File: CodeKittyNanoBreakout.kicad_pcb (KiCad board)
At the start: 2 copper layers, 17.8 x 43.2 mm, 14 parts, among them P1 CONN_01X02, P2 CONN_01X02, P3 CONN_01X03, P4 CONN_01X03, P5 CONN_01X02, SW1 SW_PUSH_SMALL_H, SW2 Switch_SPDT_x2, U1 ArduinoNano

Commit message: ...
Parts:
- added D2: D, Diodes_SMD:D_SOD-323_HandSoldering, F.Cu at (201.4, 113.5)
- added Q1: MMBT3904, TO_SOT_Packages_SMD:SOT-23, F.Cu at (210.3, 113.3)
- added R4: 1K, Resistors_SMD:R_0603_HandSoldering, F.Cu at (207.0, 113.4)
- P5: value CONN_01X02 -> CONN_01X03; footprint Pin_Headers:Pin_Header_Straight_1x02_Pitch2.54mm -> Pin_Headers:Pin_Header_Straight_1x03_Pitch2.54mm
- R1: footprint Resistors_SMD:R_0805_HandSoldering -> Resistors_SMD:R_0603_HandSoldering
- R2: footprint Resistors_SMD:R_0805_HandSoldering -> Resistors_SMD:R_0603_HandSoldering; moved to F.Cu
- SP1: value SPEAKER -> PIEZO
- moved F1 20.8 mm to (206.0, 113.9), turned to 180 degrees
- moved P5 10.5 mm to (208.9, 98.0), turned to 90 degrees
- moved G*** 9.25 mm to (205.2, 120.4)
- moved SP1 6.56 mm to (205.8, 120.9)
- moved P4 5.13 mm to (208.9, 100.6), turned to 90 degrees
- moved P3 4.13 mm to (208.9, 103.1), turned to 90 degrees
- moved P2 3.50 mm to (208.9, 95.5), turned to 90 degrees
- moved R1 1.67 mm to (210.2, 85.9), turned to 180 degrees
- moved P1 1.66 mm to (208.9, 93.0), turned to 90 degrees
- moved R2 0.92 mm to (210.2, 87.9), turned to 0 degrees
- moved U1 0.06 mm to (205.7, 104.1)
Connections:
- P5 pad 2: BUZZ -> 5V
- SP1 pad 1: BUZZ -> VCC
- SP1 pad 2: GND -> Net-(D2-Pad2)
- U1 pad 20: Net-(U1-Pad20) -> SENS
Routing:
- net Net-(F1-Pad1): track 7.31 -> 31.6 mm, vias 0 -> 4
- net Net-(D2-Pad2): track 0.00 -> 19.7 mm, vias 0 -> 1
- net GND: track 22.0 -> 7.86 mm
- net VCC: track 32.1 -> 20.9 mm
- net BUZZ: track 32.1 -> 21.1 mm, vias 1 -> 3
- net SENS: track 0.00 -> 10.4 mm, vias 0 -> 2
- net Net-(Q1-Pad1): track 0.00 -> 3.54 mm
- net RSERVO: track 15.2 -> 11.9 mm, vias 0 -> 1
- net RST: track 44.5 -> 41.7 mm, vias 2 -> 0
- net Net-(D1-Pad1): track 4.19 -> 2.31 mm
- net Net-(P1-Pad2): track 8.56 -> 6.84 mm, vias 1 -> 0
- net LSERVO: track 10.4 -> 11.7 mm, vias 0 -> 1
- net TAIL: track 3.95 -> 2.65 mm
- net 5V: track 36.8 -> 37.2 mm, vias 1 -> 2
- net Net-(P2-Pad2): track 8.66 -> 8.76 mm, vias 2 -> 0
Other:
- board text added: "CodeKitty v1.0 DM120317"
- board text removed: "-"
- board text removed: "1"
- board text removed: "BATT"
- board text removed: "CodeKitty DM100917"
- board text removed: "LEFT"
- board text removed: "RIGHT"
- board text removed: "SPKR"
- board text removed: "TAIL"

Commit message: changed DM to CK
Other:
- board text added: "CodeKitty v1.01 CK020318"
- board text removed: "CodeKitty v1.0 DM120317"
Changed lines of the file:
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@@
 (kicad_pcb (version 4) (host pcbnew 4.0.4-stable)
   (general
-    (links 32)
-    (no_connects 1)
-    (area 196.774999 82.474999 214.705001 125.805001)
+    (links 31)
+    (no_connects 0)
+    (area 194.564 75.9726 220.218001 131.9314)
     (thickness 1.6)
     (drawings 18)
@@
     (add_net LSERVO)
     (add_net "Net-(D1-Pad1)")
-    (add_net "Net-(D2-Pad1)")
     (add_net "Net-(D2-Pad2)")
     (add_net "Net-(F1-Pad1)")
@@
   (gr_line (start 210.6295 83.6295) (end 209.8675 84.3915) (layer F.SilkS) (width 0.2))
   (gr_line (start 210.6295 82.931) (end 210.6295 84.328) (layer F.SilkS) (width 0.2))
-  (gr_text "CodeKitty  v1.0 DM120317" (at 205.6384 124.6632) (layer F.Mask)
+  (gr_text "CodeKitty  v1.01 CK020318" (at 205.6384 124.6632) (layer F.Mask)
     (effects (font (size 1 0.8) (thickness 0.15)))
   )

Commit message: 1.0.2
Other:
- board text added: "CodeKitty v1.02 CK020318"
- board text removed: "CodeKitty v1.01 CK020318"
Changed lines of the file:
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@@
-(kicad_pcb (version 4) (host pcbnew 4.0.4-stable)
+(kicad_pcb (version 4) (host pcbnew 4.0.7)
   (general
     (links 31)
@@
   (gr_line (start 210.6295 83.6295) (end 209.8675 84.3915) (layer F.SilkS) (width 0.2))
   (gr_line (start 210.6295 82.931) (end 210.6295 84.328) (layer F.SilkS) (width 0.2))
-  (gr_text "CodeKitty  v1.01 CK020318" (at 205.6384 124.6632) (layer F.Mask)
+  (gr_text "CodeKitty  v1.02 CK020318" (at 205.6384 124.6632) (layer F.Mask)
     (effects (font (size 1 0.8) (thickness 0.15)))
   )

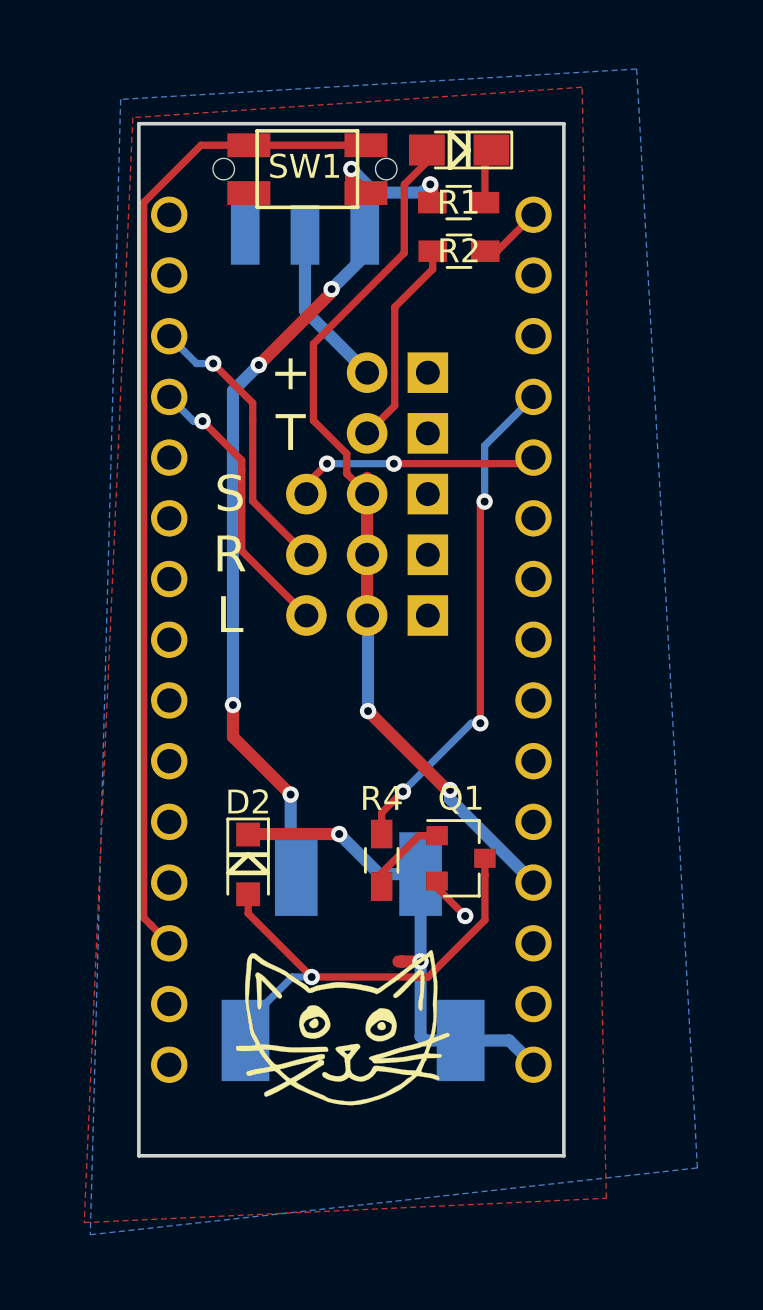
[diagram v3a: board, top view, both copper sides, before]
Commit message: removed driver from piezo -- direct drive baby!
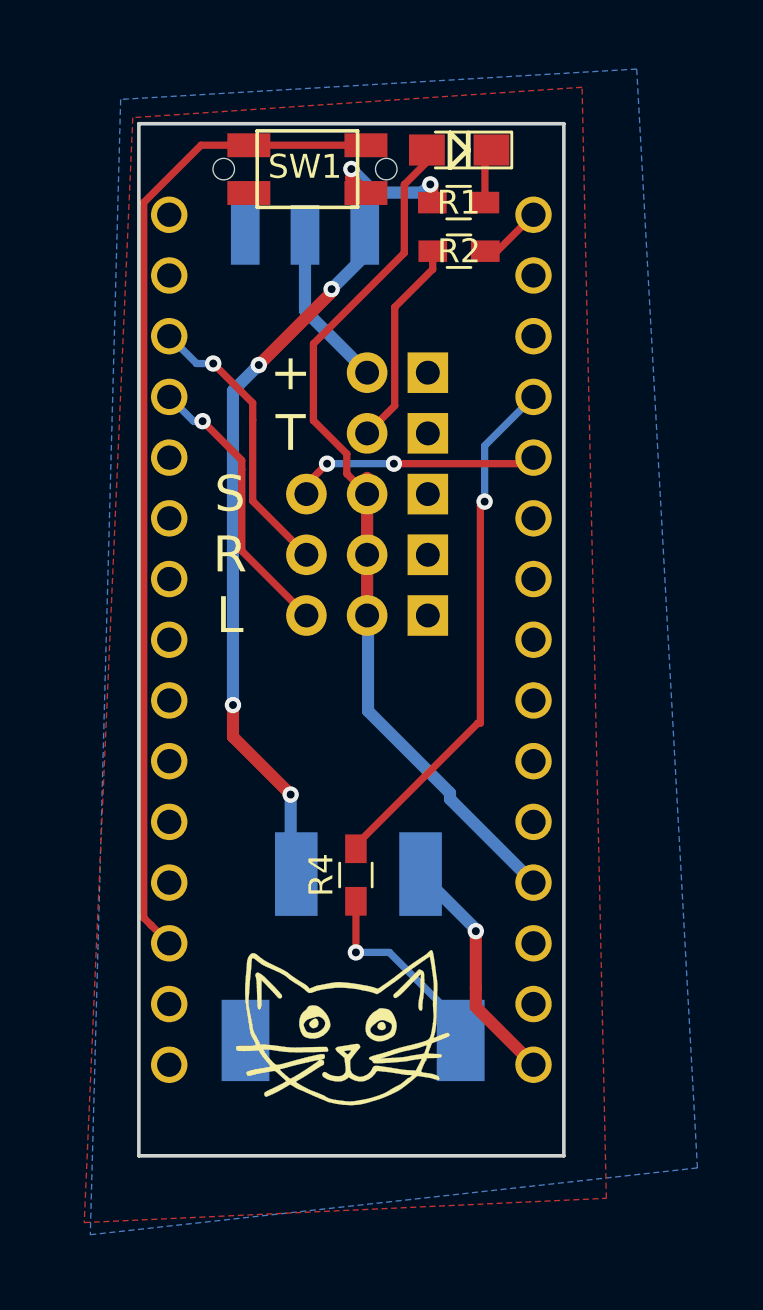
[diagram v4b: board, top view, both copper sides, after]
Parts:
- removed D2: D, Diodes_SMD:D_SOD-323_HandSoldering
- removed Q1: MMBT3904, TO_SOT_Packages_SMD:SOT-23
- moved R4 1.24 mm to (205.9, 114.0)
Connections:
- R4 pad 1: Net-(Q1-Pad1) -> Net-(R4-Pad1)
- SP1 pad 1: VCC -> Net-(R4-Pad1)
- SP1 pad 2: Net-(D2-Pad2) -> GND
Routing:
- net Net-(D2-Pad2): track 19.7 -> 0.00 mm, vias 1 -> 0
- net VCC: track 20.9 -> 11.2 mm, vias 2 -> 1
- net Net-(R4-Pad1): track 0.00 -> 8.46 mm, vias 0 -> 1
- net Net-(Q1-Pad1): track 3.54 -> 0.00 mm
- net GND: track 7.86 -> 6.61 mm, vias 3 -> 2
- net BUZZ: track 21.1 -> 22.0 mm, vias 3 -> 1
- net 5V: track 37.2 -> 37.1 mm, vias 2 -> 0
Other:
- board text added: "CodeKitty v1.0.3 CK020318"
- board text removed: "CodeKitty v1.02 CK020318"
